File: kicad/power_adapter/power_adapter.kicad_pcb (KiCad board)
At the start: 2 copper layers, 23 x 27 mm, 11 parts, among them J1 Barrel_Jack, J2 Conn_01x03_Pin, Q1 PMV65XP,215, Q2 PMV65XP,215, U1 AMS1117-5.0

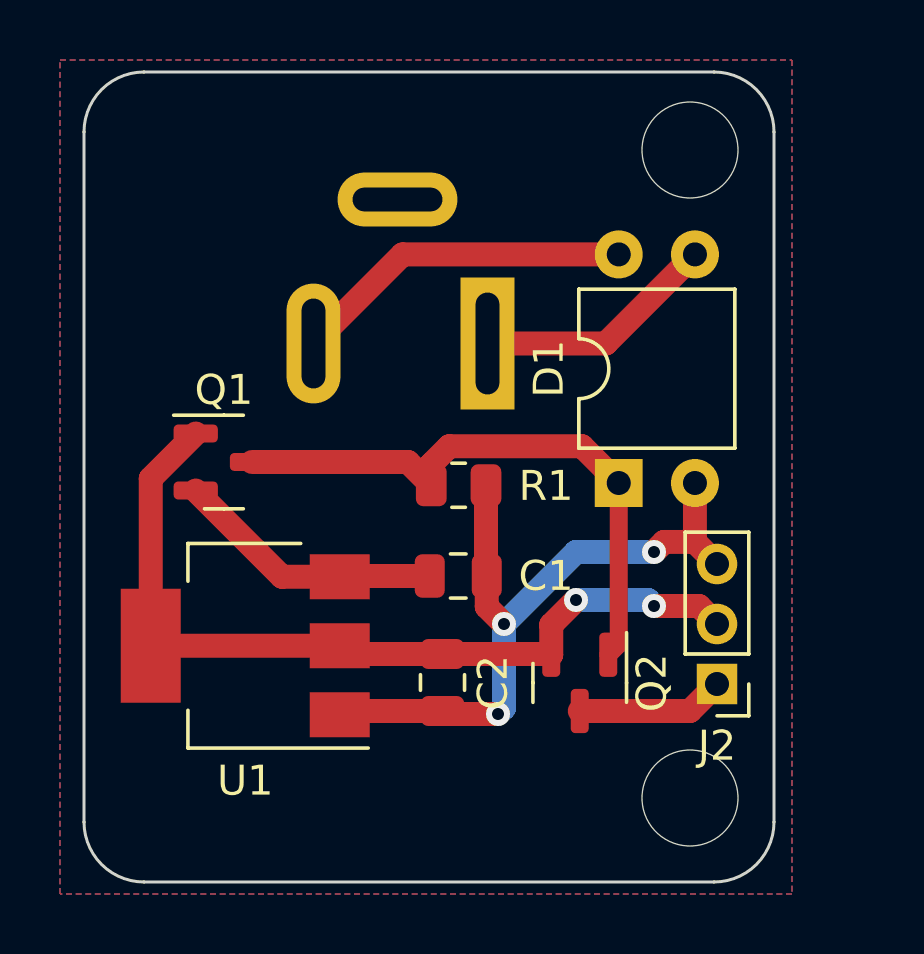
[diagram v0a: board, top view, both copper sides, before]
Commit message: Improving power adapter
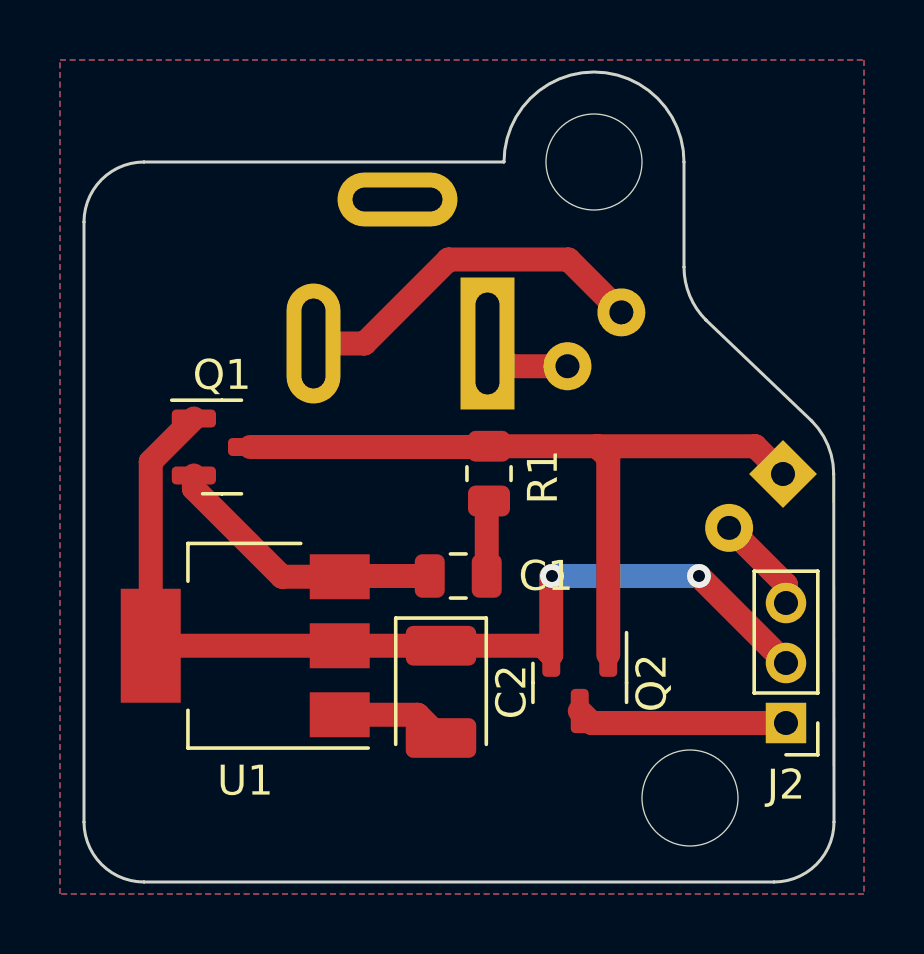
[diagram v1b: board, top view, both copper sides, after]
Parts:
- C1: value 0.33uF -> 10uF
- C2: value 0.1uF -> 22uF; footprint Capacitor_SMD:C_0805_2012Metric -> Capacitor_Tantalum_SMD:CP_EIA-3528-21_Kemet-B
- D1: moved to B.Cu
- moved D1 5.48 mm to (145.3, 97.4), turned to 135 degrees
- moved REF** 3.22 mm to (139.0, 87.0)
- moved J2 2.64 mm to (145.4, 105.7)
- moved R1 1.08 mm to (135.5, 97.4), turned to 90 degrees
- moved Q1 0.50 mm to (126.6, 96.5)
- moved C2 0.32 mm to (133.9, 104.7)
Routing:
- net GND: track 23.8 -> 9.52 mm, vias 3 -> 0
- net +9V: track 19.9 -> 25.3 mm
- net Net-(D1-Pad3): track 8.15 -> 2.98 mm
- net +5V: track 28.4 -> 33.3 mm
- net VBUS: track 4.95 -> 7.04 mm
- net Net-(D1-Pad4): track 11.4 -> 12.2 mm
- net Net-(Q1-S): track 9.00 -> 9.53 mm
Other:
- board size 23 x 27 mm -> 25 x 27 mm

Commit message: Power adapter fixes
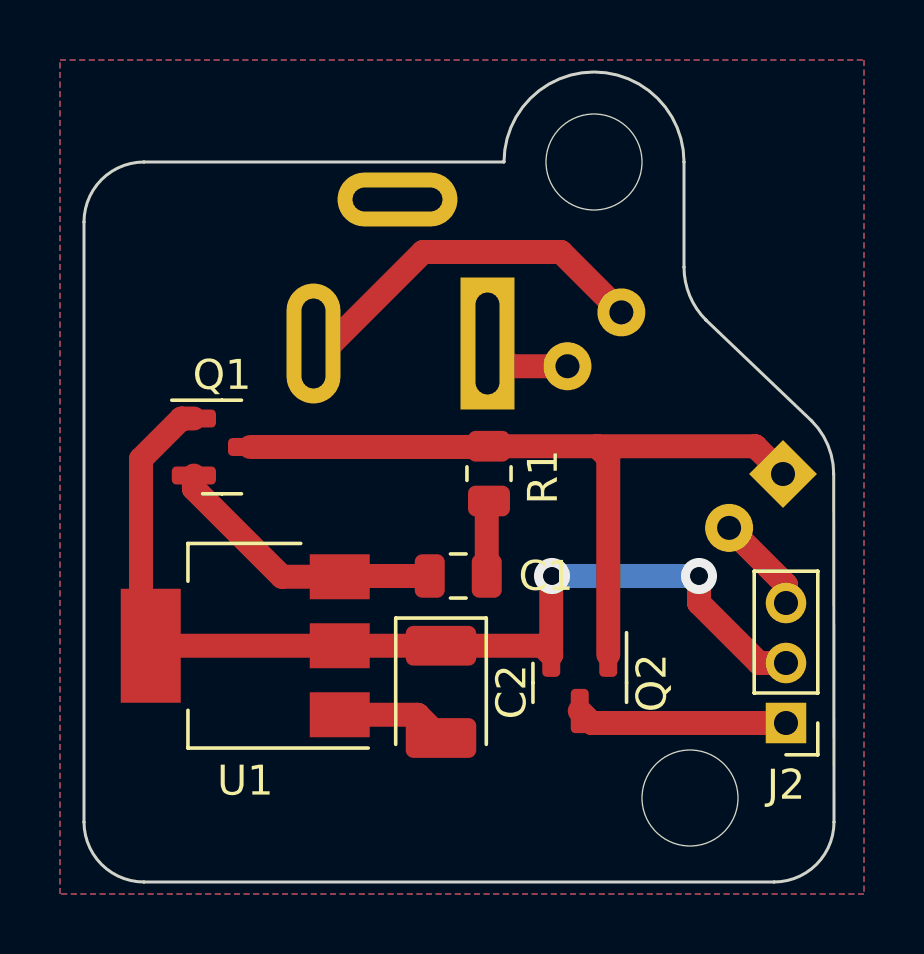
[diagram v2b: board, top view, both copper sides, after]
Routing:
- net +5V: track 33.3 -> 34.3 mm
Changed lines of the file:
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@@
   (segment (start 145.4 101.7) (end 145.4 101.092102) (width 0.8) (layer "F.Cu") (net 2))
   (segment (start 130.525 105.425) (end 133.125 105.425) (width 0.8) (layer "F.Cu") (net 2))
+  (segment (start 125.25 95.55) (end 123.9 96.9) (width 0.8) (layer "F.Cu") (net 3))
+  (segment (start 142.5 100.8) (end 142.5 101.7) (width 0.8) (layer "F.Cu") (net 3))
+  (segment (start 144.5 103.7) (end 145.4 103.7) (width 0.8) (layer "F.Cu") (net 3))
   (segment (start 124.225 103.125) (end 130.525 103.125) (width 0.8) (layer "F.Cu") (net 3))
   (segment (start 130.525 103.125) (end 133.9 103.125) (width 0.8) (layer "F.Cu") (net 3))
-  (segment (start 142.5 100.8) (end 145.4 103.7) (width 0.8) (layer "F.Cu") (net 3))
+  (segment (start 125.6625 95.55) (end 125.25 95.55) (width 0.8) (layer "F.Cu") (net 3))
+  (segment (start 123.9 102.8) (end 124.225 103.125) (width 0.8) (layer "F.Cu") (net 3))
   (segment (start 137.6 100.8) (end 137.575 100.825) (width 0.8) (layer "F.Cu") (net 3))
   (segment (start 137.575 100.825) (end 137.575 103.425) (width 0.8) (layer "F.Cu") (net 3))
   (segment (start 137.275 103.125) (end 137.575 103.425) (width 0.8) (layer "F.Cu") (net 3))
-  (segment (start 125.6625 95.55) (end 124.225 96.9875) (width 0.8) (layer "F.Cu") (net 3))
-  (segment (start 124.225 96.9875) (end 124.225 103.125) (width 0.8) (layer "F.Cu") (net 3))
+  (segment (start 142.5 101.7) (end 144.5 103.7) (width 0.8) (layer "F.Cu") (net 3))
+  (segment (start 123.9 96.9) (end 123.9 102.8) (width 0.8) (layer "F.Cu") (net 3))
   (segment (start 133.9 103.125) (end 137.275 103.125) (width 0.8) (layer "F.Cu") (net 3))
-  (via (at 142.5 100.8) (size 0.8) (drill 0.4) (layers "F.Cu" "B.Cu") (net 3))
-  (via (at 137.6 100.8) (size 0.8) (drill 0.4) (layers "F.Cu" "B.Cu") (net 3))
+  (via (at 142.5 100.8) (size 1.2) (drill 0.6) (layers "F.Cu" "B.Cu") (net 3))
+  (via (at 137.6 100.8) (size 1.2) (drill 0.6) (layers "F.Cu" "B.Cu") (net 3))
   (segment (start 142.5 100.8) (end 137.6 100.8) (width 0.8) (layer "B.Cu") (net 3))
   (segment (start 145.3 97.4) (end 144.375 96.475) (width 0.8) (layer "F.Cu") (net 4))
@@
   (segment (start 138.115795 93.807898) (end 136.207898 93.807898) (width 0.8) (layer "F.Cu") (net 5))
   (segment (start 136.207898 93.807898) (end 135.45 93.05) (width 0.8) (layer "F.Cu") (net 5))
-  (segment (start 129.65 93.05) (end 131.35 93.05) (width 0.8) (layer "F.Cu") (net 6))
-  (segment (start 138.15 90.25) (end 139.911846 92.011846) (width 0.8) (layer "F.Cu") (net 6))
-  (segment (start 134.15 90.25) (end 138.15 90.25) (width 0.8) (layer "F.Cu") (net 6))
-  (segment (start 131.35 93.05) (end 134.15 90.25) (width 0.8) (layer "F.Cu") (net 6))
+  (segment (start 129.65 93.05) (end 130.25 93.05) (width 0.8) (layer "F.Cu") (net 6))
+  (segment (start 130.25 93.05) (end 133.3 90) (width 0.8) (layer "F.Cu") (net 6))
+  (segment (start 133.3 90) (end 137.9 90) (width 0.8) (layer "F.Cu") (net 6))
+  (segment (start 137.9 90) (end 139.911846 92.011846) (width 0.8) (layer "F.Cu") (net 6))
   (segment (start 138.925 105.7) (end 138.525 105.3) (width 0.8) (layer "F.Cu") (net 7))
   (segment (start 145.4 105.7) (end 138.925 105.7) (width 0.8) (layer "F.Cu") (net 7))

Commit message: Power adapter fixes
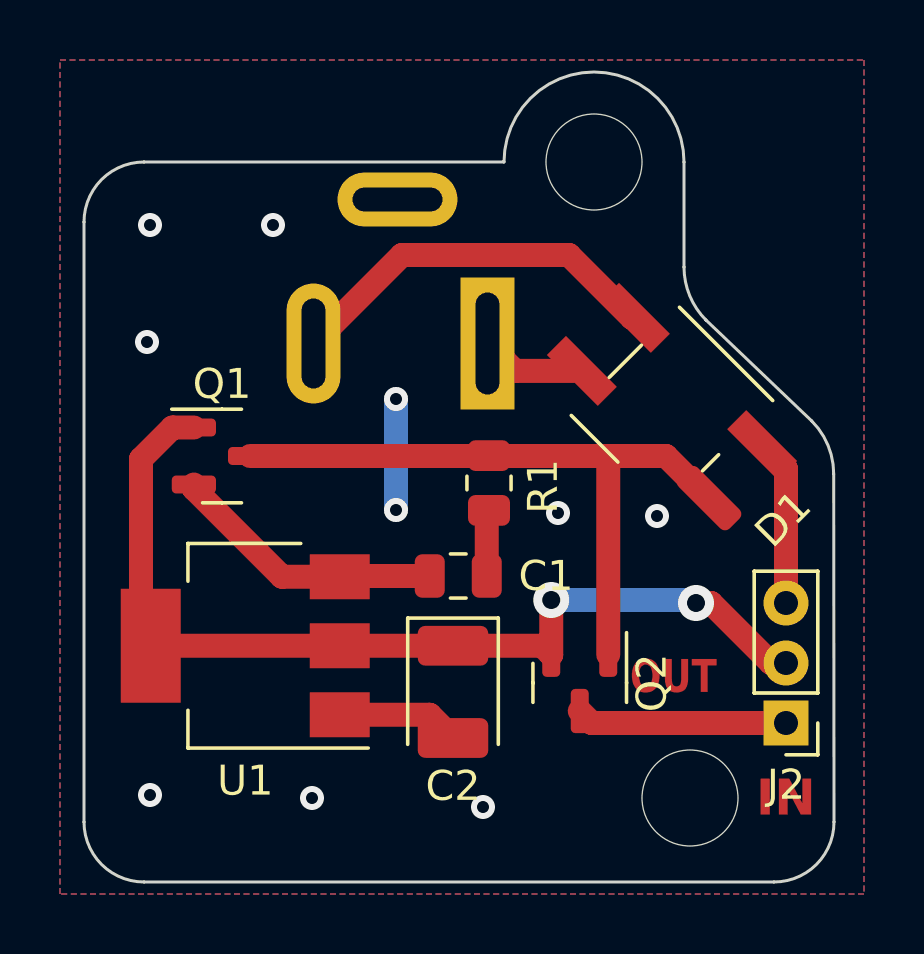
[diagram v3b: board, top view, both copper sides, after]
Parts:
- D1: footprint Package_DIP:DIP-4_W7.62mm -> lib:Diode_Bridge_MBS; moved to F.Cu
- moved D1 4.30 mm to (141.6, 95.2), turned to -135 degrees
- moved C2 0.40 mm to (134.3, 104.7)
- moved R1 0.31 mm to (135.5, 97.7)
- moved Q1 0.30 mm to (126.6, 96.8)
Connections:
- J1 pad 1: Net-(D1-Pad3) -> Net-(D1-Pad4)
- J1 pad 2: Net-(D1-Pad4) -> Net-(D1-Pad3)
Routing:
- net Net-(D1-Pad3): track 2.98 -> 12.8 mm
- net Net-(D1-Pad4): track 12.4 -> 3.52 mm
- net GND: track 9.52 -> 15.6 mm, vias 0 -> 10
- net +9V: track 25.3 -> 23.3 mm
- net +5V: track 34.3 -> 32.6 mm
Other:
- board text added: "+5V (out)"
- board text added: "GND"
- board text added: "IN"
- board text added: "OUT"
- board text added: "USB VBUS (in)"
